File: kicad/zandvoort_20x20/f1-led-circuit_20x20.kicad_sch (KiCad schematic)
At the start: 43 parts, among them J1 USB_C_Receptacle_USB2.0_14P, Q1 TSM085P03CV_RGG, SW2 SW_SPST, SW3 SW_SPDT, U1 HD108-2020, U2 HD108-2020, U3 HD108-2020, U300 ESP32-C3-MINI-1, U301 MCP9701AT-E/LT, U302 LDLN050, U303 NUF2042XV6T1G, U4 HD108-2020, U5 HD108-2020, U6 HD108-2020

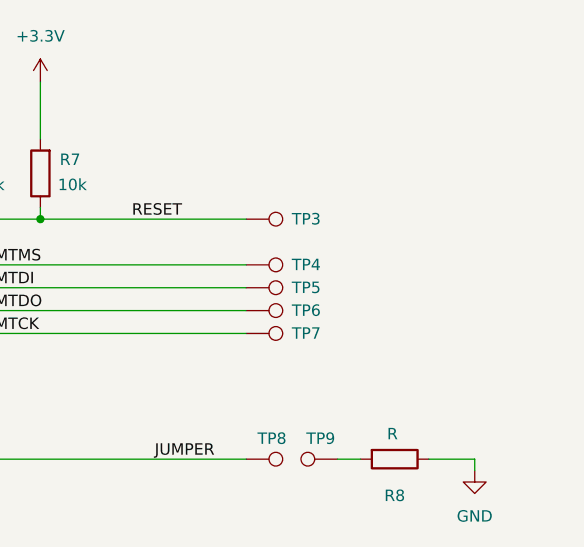
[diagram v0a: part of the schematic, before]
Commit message: Add to test points +3.3V and GND
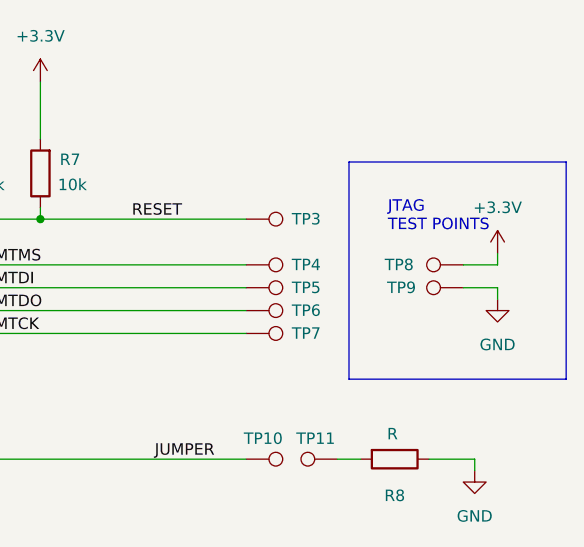
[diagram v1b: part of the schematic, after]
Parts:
- added TP8, TP9: TestPoint, TestPoint:TestPoint_Pad_D1.5mm, symbol Connector:TestPoint
- renumbered TP8 to TP10, TP9 to TP11
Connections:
- net +3.3V: now also TP8.1
- net GND: now also TP9.1
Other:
- note added: "JTAG TEST POINTS"

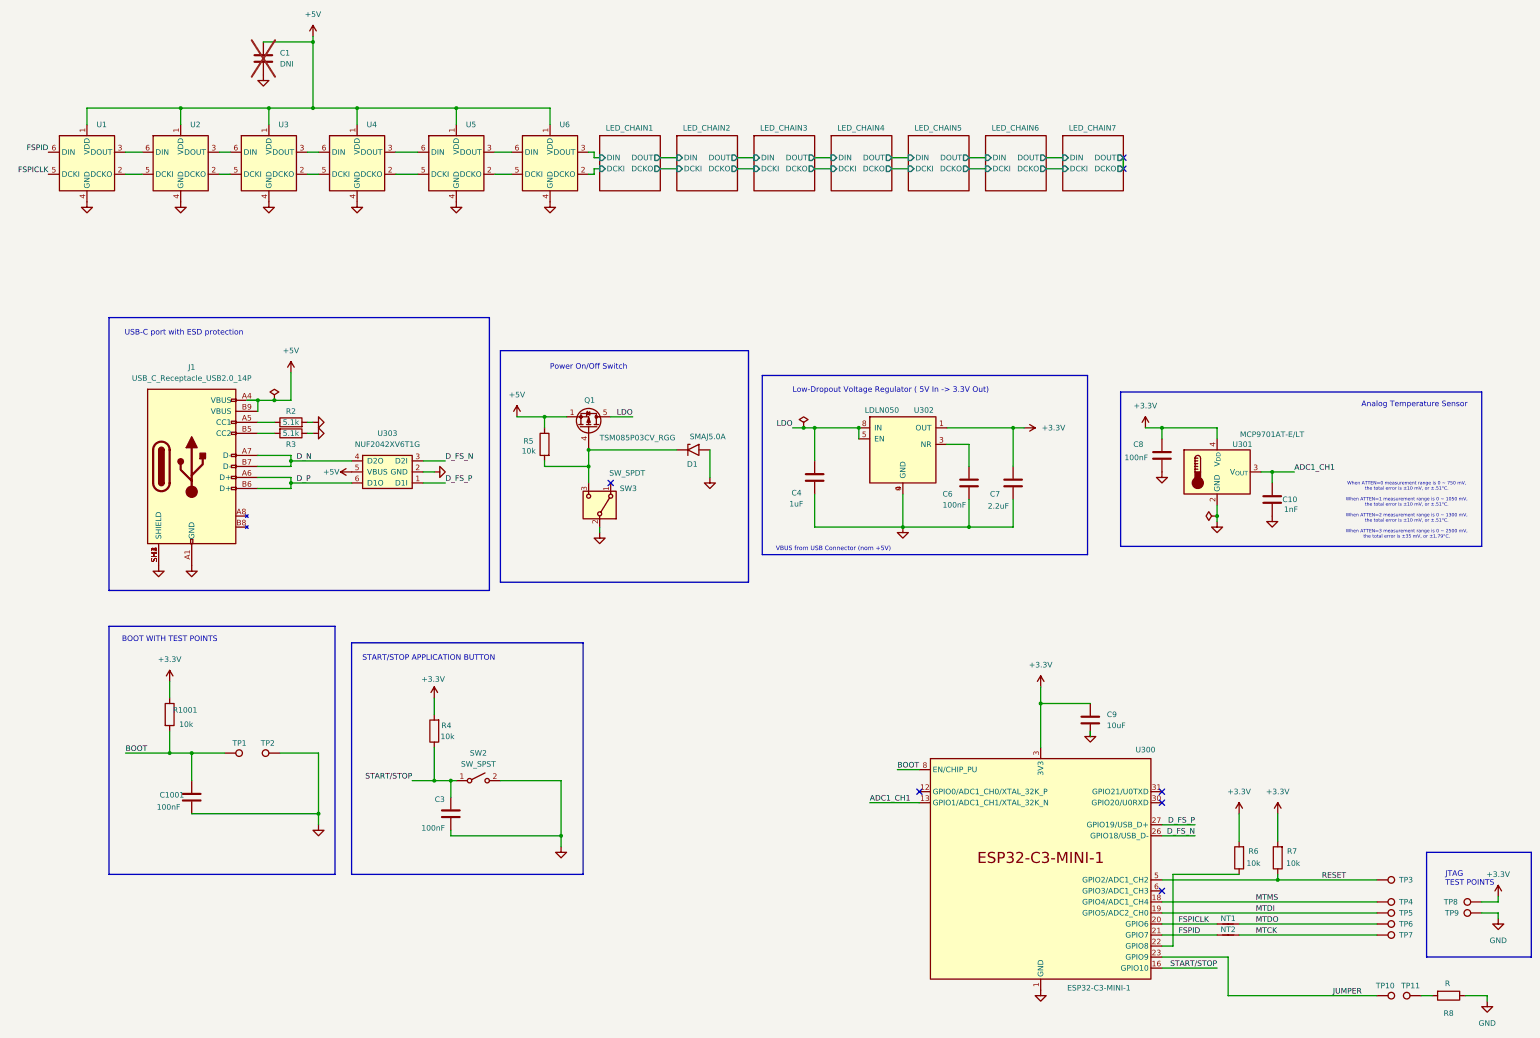
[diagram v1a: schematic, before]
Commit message: Remove power switch from schematic
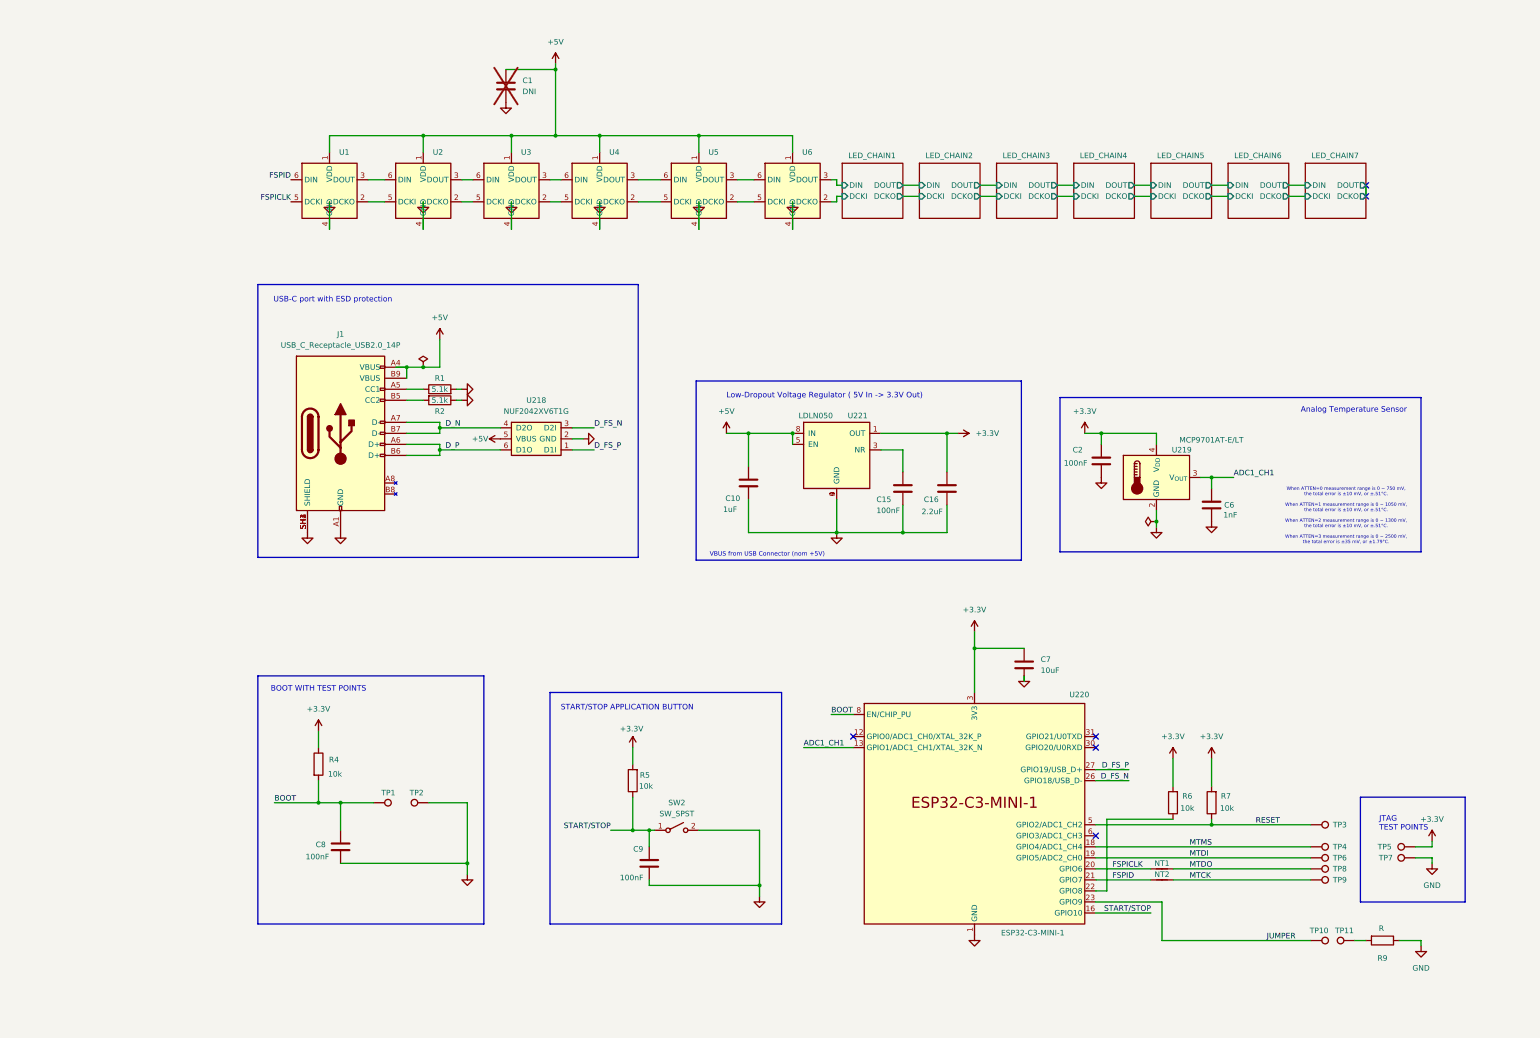
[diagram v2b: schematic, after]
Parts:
- removed C4: 1uF, Capacitor_SMD:C_0402_1005Metric, symbol Device:C
- removed C6: 100nF, Capacitor_SMD:C_0402_1005Metric, symbol Device:C
- removed C7: 2.2uF, Capacitor_SMD:C_0402_1005Metric, symbol Device:C
- removed D1: SMAJ5.0A, Diode_SMD:D_SMA, symbol Diode:SMAJ5.0A
- removed Q1: TSM085P03CV_RGG, F1-LED-CIRCUIT-LIBRARY:PDFN33-1EP_3x3mm_P0.65mm, symbol Jitter_Symbols:TSM085P03CV_RGG
- removed R5: 10k, Resistor_SMD:R_0402_1005Metric, symbol Device:R
- removed SW3: SW_SPDT, F1-LED-CIRCUIT-LIBRARY:AS12AP_NKK, symbol Switch:SW_SPDT
- removed U302: LDLN050, F1-LED-CIRCUIT-LIBRARY:DFN8_LDLN050_STM, symbol F1-LED-CIRCUIT-LIBRARY:LDLN050
- added C10: 1uF, Capacitor_SMD:C_0402_1005Metric, symbol Device:C
- added C15: 100nF, Capacitor_SMD:C_0402_1005Metric, symbol Device:C
- added C16: 2.2uF, Capacitor_SMD:C_0402_1005Metric, symbol Device:C
- added U221: LDLN050, F1-LED-CIRCUIT-LIBRARY:DFN8_LDLN050_STM, symbol F1-LED-CIRCUIT-LIBRARY:LDLN050
- renumbered C8 to C2, C10 to C6, C9 to C7, C1001 to C8, C3 to C9, R2 to R1, R3 to R2, R1001 to R4, R4 to R5, R8 to R9, TP8 to TP5, TP5 to TP6, TP9 to TP7, TP6 to TP8, TP7 to TP9, U303 to U218, U301 to U219, U300 to U220
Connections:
- net +3.3V: now also C16.1, U221.1 (OUT)
- net +5V: now also C10.1, U221.5 (EN), U221.8 (IN)
- net GND: now also C10.2, C15.2, C16.2, U221.4 (GND), U221.9 (GND)
- new net: C15.1, U221.3 (NR)
- no-connect marks 7 -> 6
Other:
- note removed: "Power On/Off Switch"
- moved on the sheet: C1, C2, C6, C7, C8, C9, J1, NT1, NT2, R1, R2, R4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

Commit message: Annotate schematic again and update PCB layout
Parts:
- renumbered C10 to C3, C15 to C4, C16 to C5, R4 to R3, R5 to R4, R6 to R5, R7 to R6, R9 to R7, SW2 to SW1, U220 to U300, U219 to U301, U221 to U302, U218 to U303
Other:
- moved on the sheet: C1, C2, C3, C4, C5, C6, C7, C8, C9, J1, NT1, NT2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
